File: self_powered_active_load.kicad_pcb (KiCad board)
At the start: 2 copper layers, 220 x 99.8 mm, 90 parts, among them J1 Conn_01x05, J2 Conn_01x03, J3 BANANA_CONN, J4 BANANA_CONN, Q1 2SC4117, Q10 BDW94CFP, Q11 2SC4117, Q12 BDW94CFP, Q13 2SC4117, Q14 BDW94CFP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

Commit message: Name added on PCB
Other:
- board text added: "Dr. Frank Kirschbaum 2023"
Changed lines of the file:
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@@
   (gr_line (start 259.334 145.64) (end 259.334 45.79)
     (stroke (width 0.15) (type solid)) (layer "Edge.Cuts"))
+  (gr_text "Dr. Frank Kirschbaum 2023" (at 246.25 144.75) (layer "B.SilkS")
+    (effects (font (size 1 1) (thickness 0.15)) (justify left bottom mirror))
+  )
+  (gr_text "Dr. Frank Kirschbaum 2023" (at 225.25 144.75) (layer "F.SilkS")
+    (effects (font (size 1 1) (thickness 0.15)) (justify left bottom))
+  )
   (segment (start 228.092 133.81) (end 231.212166 133.81) (width 0.25) (layer "F.Cu") (net 1))
   (segment (start 237.4275 133.7975) (end 237.49 133.735) (width 0.25) (layer "F.Cu") (net 1))

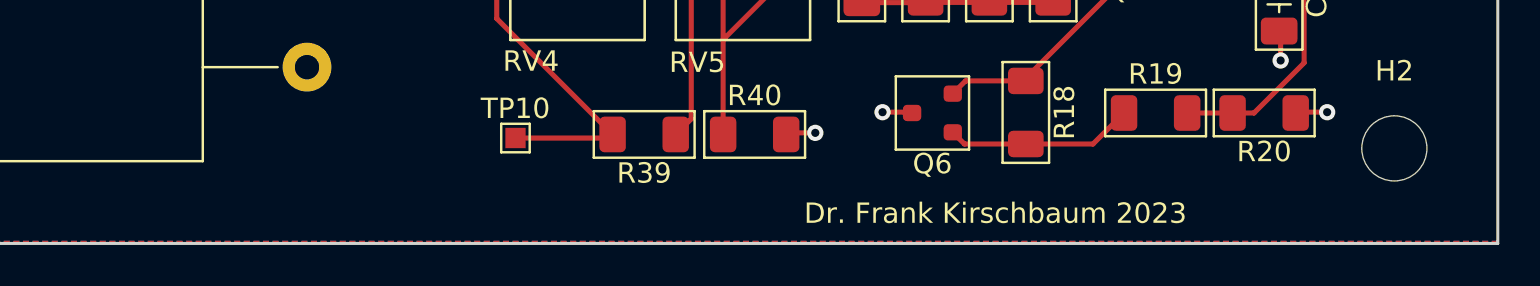
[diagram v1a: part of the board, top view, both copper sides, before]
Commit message: Name on PCB edited
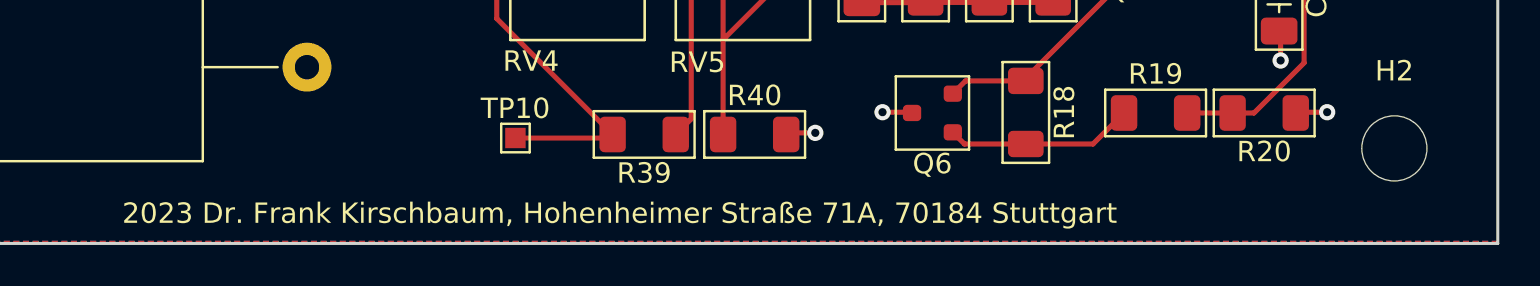
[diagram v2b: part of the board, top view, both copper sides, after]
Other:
- board text added: "2023 Dr. Frank Kirschbaum, Hohenheimer Straße 71A, 70184 Stuttgart"
- board text removed: "Dr. Frank Kirschbaum 2023"
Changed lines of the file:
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@@
   (gr_line (start 259.334 145.64) (end 259.334 45.79)
     (stroke (width 0.15) (type solid)) (layer "Edge.Cuts"))
-  (gr_text "Dr. Frank Kirschbaum 2023" (at 246.25 144.75) (layer "B.SilkS")
+  (gr_text "2023 Dr. Frank Kirschbaum, Hohenheimer Straße 71A, 70184 Stuttgart" (at 246.25 144.75) (layer "B.SilkS")
     (effects (font (size 1 1) (thickness 0.15)) (justify left bottom mirror))
   )
-  (gr_text "Dr. Frank Kirschbaum 2023" (at 225.25 144.75) (layer "F.SilkS")
+  (gr_text "2023 Dr. Frank Kirschbaum, Hohenheimer Straße 71A, 70184 Stuttgart" (at 191.75 144.75) (layer "F.SilkS")
     (effects (font (size 1 1) (thickness 0.15)) (justify left bottom))
   )

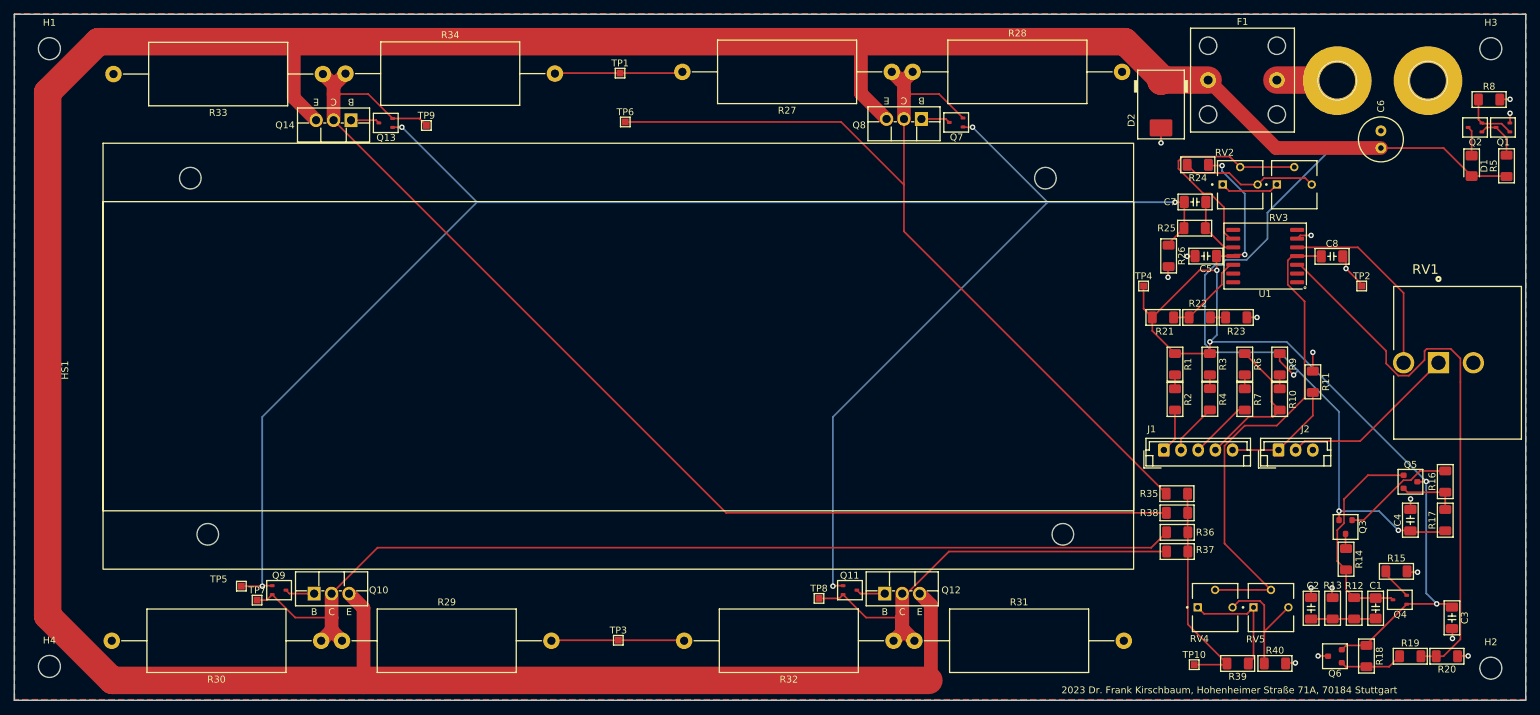
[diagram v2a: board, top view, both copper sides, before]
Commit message: via stitching added
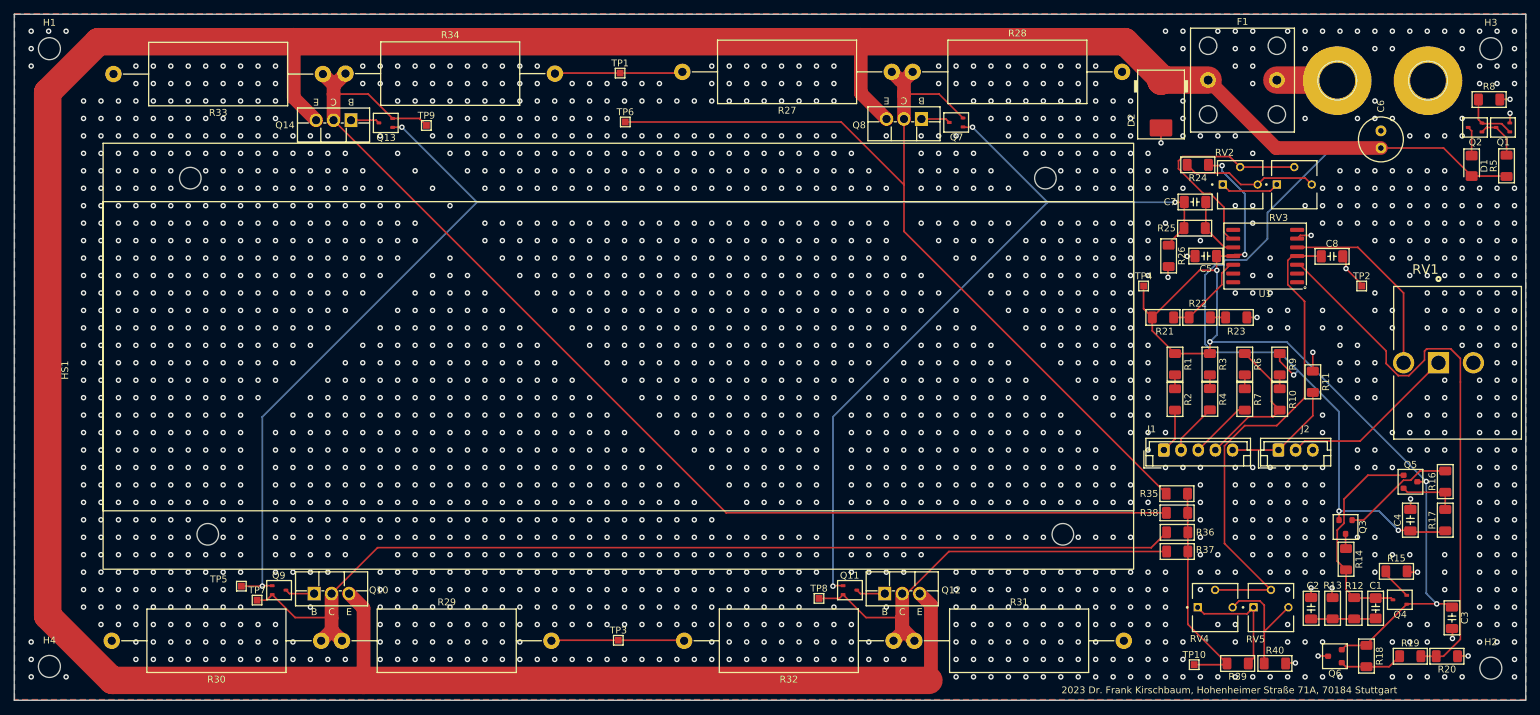
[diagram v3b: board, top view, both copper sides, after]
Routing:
- net GNDA: vias 17 -> 2158
